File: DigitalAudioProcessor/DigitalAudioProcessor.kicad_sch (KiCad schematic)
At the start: 65 parts, among them J1 SWD, J2 I2S_OUT, J3 I2S_1, J4 USB, J5 I2S_3, J6 I2C, J7 I2S_2, J8 3.3V, U1 TOSLINK_RX, U2 USBLC6-2SC6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

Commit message: DigitalAudioProcessor net labels
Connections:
- net I2S_2_DATA: now reaches R13.1, TP15.1, U3.38 (PB14)
- net I2S_2_BCK: now reaches R12.1, TP14.1, U3.32 (PB10)
- net DEBUG_RX: now reaches TP12.1, U3.64 (PB8)
- net I2S_1_BCK: now reaches R6.1, TP4.1, U3.24 (PA5)
- net I2S_OUT_DATA: now reaches R4.1, TP2.1, U3.17 (PA0)
- net I2S_1_DATA: now reaches R7.1, TP5.1, U3.25 (PA6)
- net I2S_1_LRCK: now reaches R8.1, TP6.1, U3.23 (PA4)
- net I2S_2_LRCK: now reaches R14.1, TP16.1, U3.36 (PB12)
- net I2C_~{INT}: now reaches J6.3 (Pin_3), TP11.1, U3.60 (PB5)
- net I2C_SCL: now reaches J6.1 (Pin_1), U3.61 (PB6)
- net I2C_SDA: now reaches J6.2 (Pin_2), U3.62 (PB7)
- net USB_VBUS: now reaches J4.1 (Pin_1), U2.5 (VBUS), U3.44 (PA9)
- net I2S_OUT_BCK: now reaches R3.1, TP1.1, U3.19 (PA2)
- net SPDIF_IN: now reaches C14.1, TP7.1, U1.1 (OUT), U3.27 (PC4)
- net USB_D-: now reaches U2.6 (I/O1), U3.46 (PA11)
- net USB_D+: now reaches U2.4 (I/O2), U3.47 (PA12)
- net I2S_3_BCK: now reaches R9.1, TP8.1, U3.54 (PC10)
- net I2S_3_DATA: now reaches R10.1, TP9.1, U3.55 (PC11)
- net DEBUG_TX: now reaches TP13.1, U3.65 (PB9)
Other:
- moved on the sheet: TP2

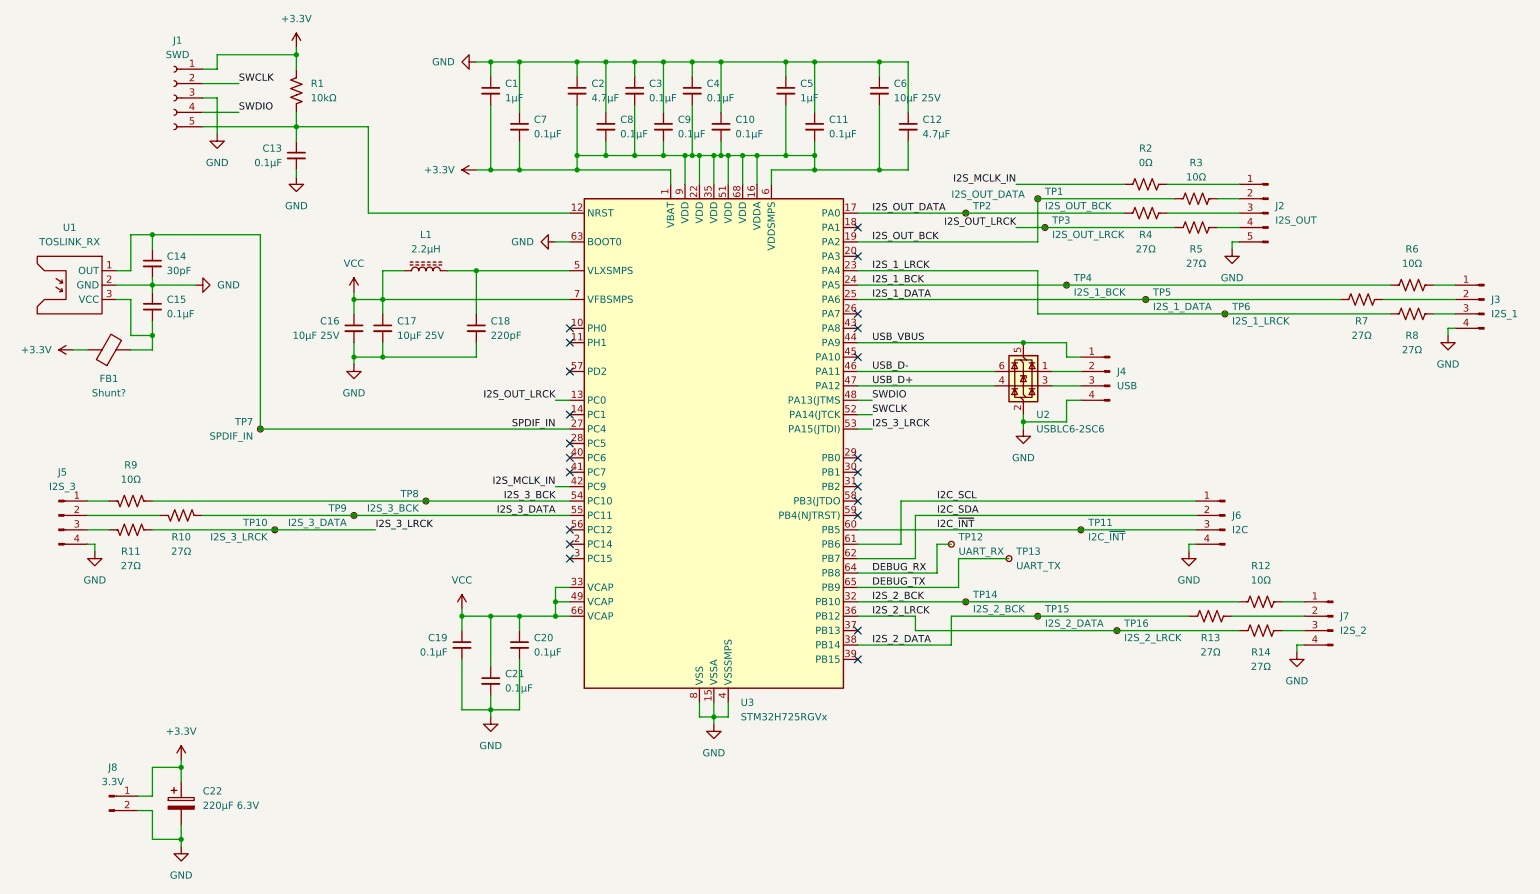
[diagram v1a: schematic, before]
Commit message: DigitalAudioProcessor fixed USB disconnect detection
Pull-down on the USB_VBUS line is required to consistently detect disconnection.
Firmware adjusted to not flush buffer on disconnect, as that causes a long freeze - seems to work fine without it too.
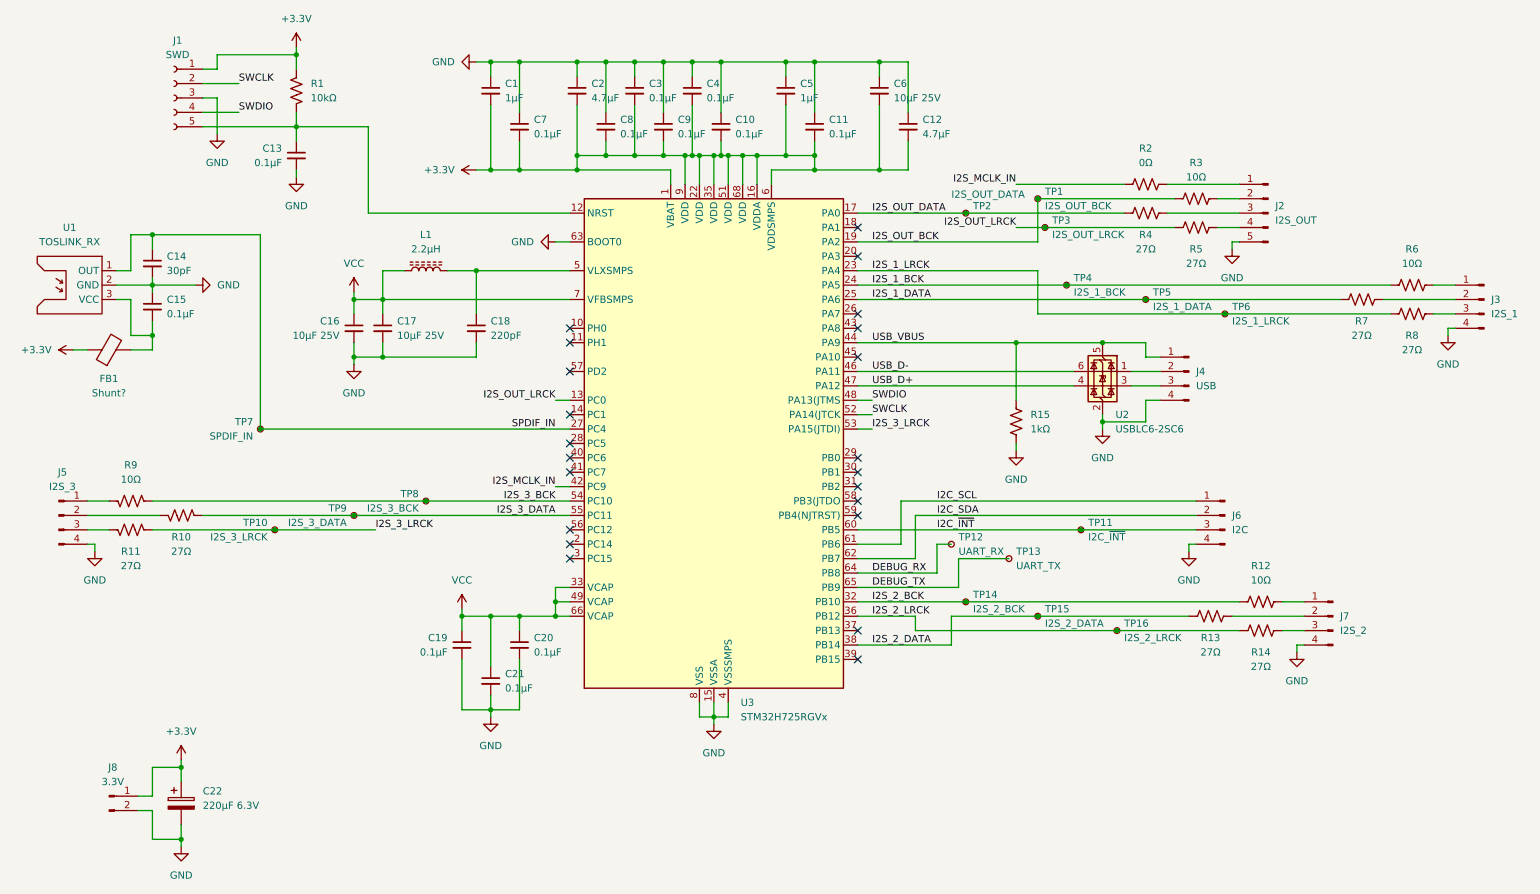
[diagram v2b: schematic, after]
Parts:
- added R15: 1kΩ, Resistor_SMD:R_0603_1608Metric, symbol Device:R_US
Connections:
- net GND: now also R15.1
- net USB_VBUS: now also R15.2
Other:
- moved on the sheet: J4, U2
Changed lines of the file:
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@@
 (kicad_sch
-	(version 20231120)
+	(version 20250114)
 	(generator "eeschema")
-	(generator_version "8.0")
+	(generator_version "9.0")
 	(paper "A4")
